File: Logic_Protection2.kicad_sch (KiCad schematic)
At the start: 18 parts

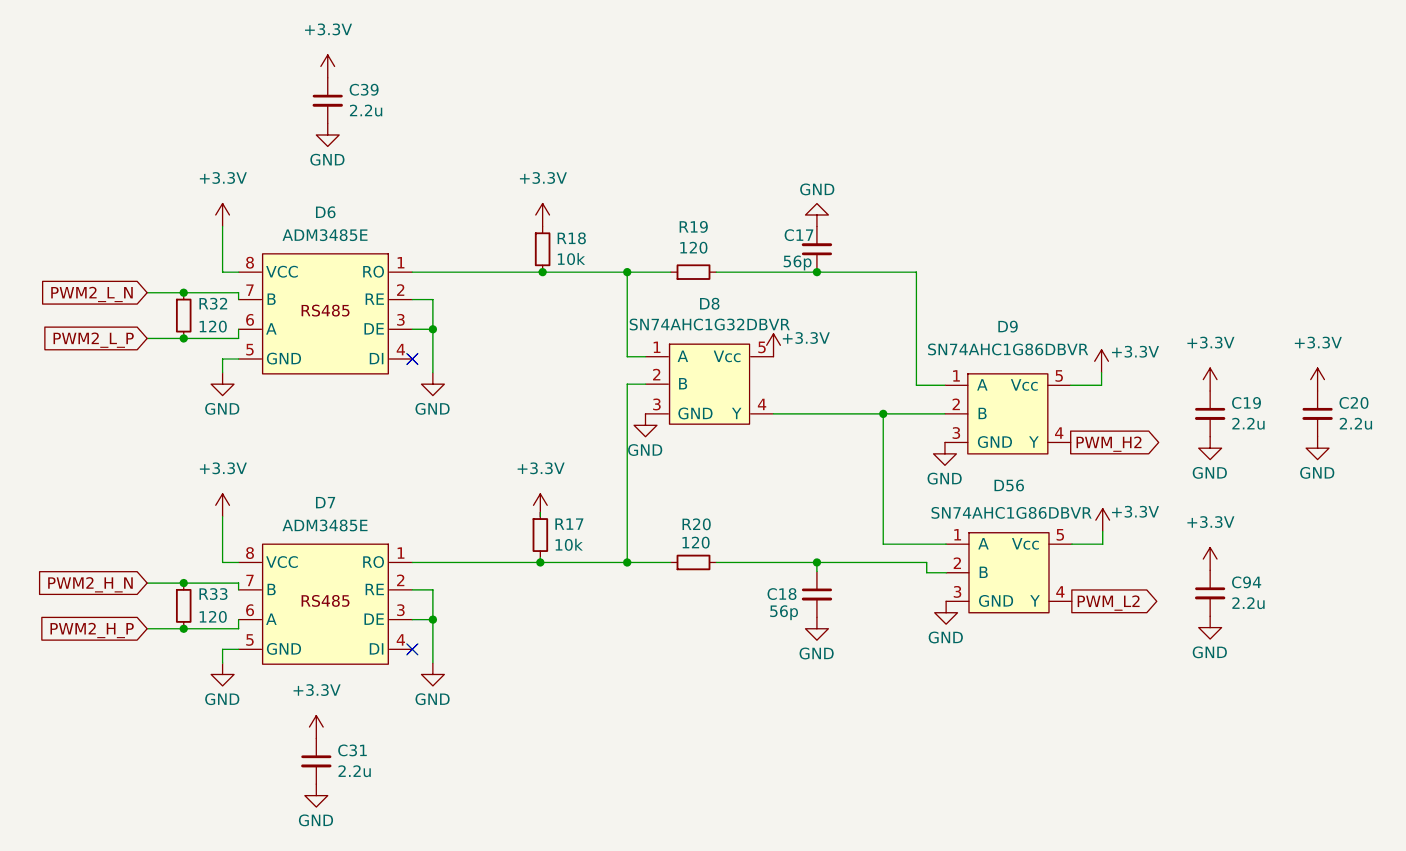
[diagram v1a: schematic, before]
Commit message: Изменил схему
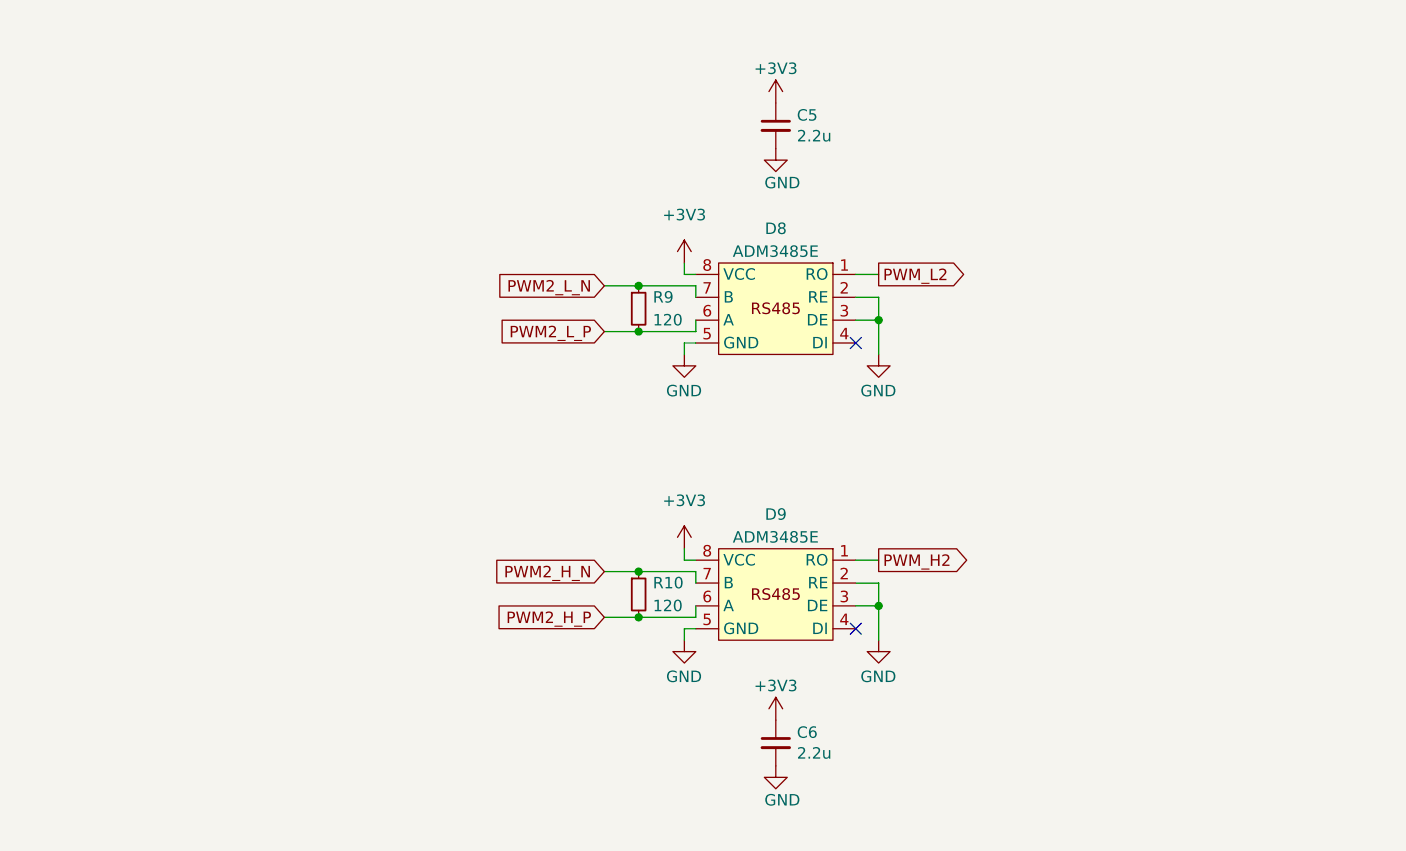
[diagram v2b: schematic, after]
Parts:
- removed C17, C18: 56p, Capacitor_SMD:C_0805_2012Metric_Pad1.18x1.45mm_HandSolder, symbol Device:C_Small
- removed C19, C20, C31, C39, C94: 2.2u, Capacitor_SMD:C_0805_2012Metric_Pad1.18x1.45mm_HandSolder, symbol Device:C_Small
- removed D56, D9: SN74AHC1G86DBVR, Package_TO_SOT_SMD:SOT-23-5_HandSoldering, symbol Logic:SN74AHC1G86DBVR
- removed D6, D7: ADM3485E, Package_SO:SOIC-8_3.9x4.9mm_P1.27mm, symbol Interface_My:ADM3485E
- removed D8: SN74AHC1G32DBVR, Package_TO_SOT_SMD:SOT-23-5_HandSoldering, symbol Logic:SN74AHC1G86DBVR
- removed R17, R18: 10k, Resistor_SMD:R_0805_2012Metric_Pad1.20x1.40mm_HandSolder, symbol Device:R_Small
- removed R19, R20, R32, R33: 120, Resistor_SMD:R_0805_2012Metric_Pad1.20x1.40mm_HandSolder, symbol Device:R_Small
- added C5, C6: 2.2u, Capacitor_SMD:C_0805_2012Metric_Pad1.18x1.45mm_HandSolder, symbol Device:C_Small
- added D8, D9: ADM3485E, Package_SO:SOIC-8_3.9x4.9mm_P1.27mm, symbol Interface_My:ADM3485E_1
- added R10, R9: 120, Resistor_SMD:R_0805_2012Metric_Pad1.20x1.40mm_HandSolder, symbol Device:R_Small
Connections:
- net +3V3: now also C5.1, C6.1, D8.8 (VCC), D9.8 (VCC)
- net GND: now also C5.2, C6.2, D8.2 (RE), D8.3 (DE), D8.5 (GND), D9.2 (RE), D9.3 (DE), D9.5 (GND)
- net PWM2_H_N: now also D9.7 (B), R10.1
- net PWM2_H_P: now also D9.6 (A), R10.2
- net PWM2_L_N: now also D8.7 (B), R9.1
- net PWM2_L_P: now also D8.6 (A), R9.2
- net PWM_H2: now also D9.1 (RO)
- net PWM_L2: now also D8.1 (RO)

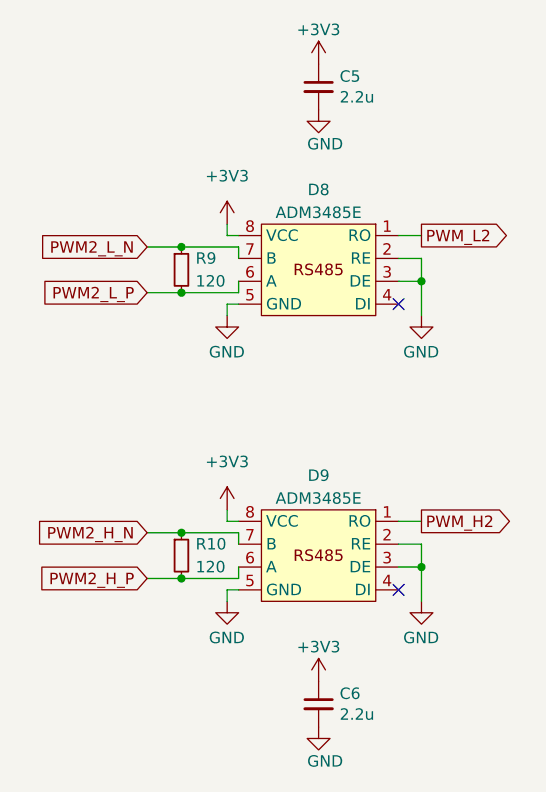
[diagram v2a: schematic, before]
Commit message: Убрал питание 3.3В
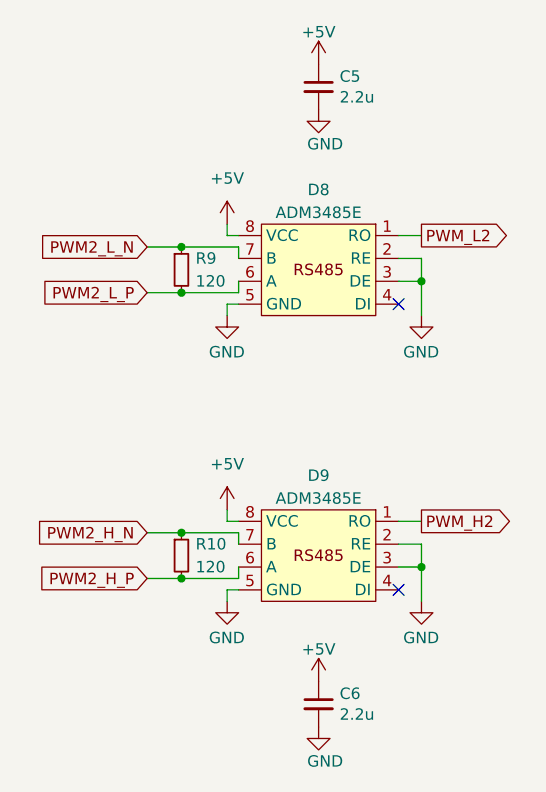
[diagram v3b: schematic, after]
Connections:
- net +3V3 renamed +5V
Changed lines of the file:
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@@
 	)
 	(symbol
-		(lib_id "power:+3.3V")
+		(lib_id "power:+5V")
 		(at 153.67 127 0)
 		(unit 1)
@@
 		(on_board yes)
 		(dnp no)
-		(property "Reference" "#PWR042"
+		(property "Reference" "#PWR42"
 			(at 153.67 130.81 0)
 			(effects
@@
 			)
 		)
-		(property "Value" "+3V3"
-			(at 153.67 123.19 0)
+		(property "Value" "+5V"
+			(at 153.67 123.444 0)
 			(effects
 				(font
@@
 			)
 		)
-		(property "Description" ""
+		(property "Description" "Power symbol creates a global label with name \"+5V\""
 			(at 153.67 127 0)
 			(effects
@@
 			(project "Adapter"
 				(path "/e63e39d7-6ac0-4ffd-8aa3-1841a4541b55/d144a014-f04c-4a5c-ab89-4d35bea7c7d6"
-					(reference "#PWR042")
-					(unit 1)
-				)
-			)
-		)
-	)
-	(symbol
-		(lib_id "power:+3.3V")
+					(reference "#PWR42")
+					(unit 1)
+				)
+			)
+		)
+	)
+	(symbol
+		(lib_id "power:+5V")
 		(at 143.51 76.2 0)
 		(unit 1)
@@
 		(dnp no)
 		(fields_autoplaced yes)
-		(property "Reference" "#PWR017"
+		(property "Reference" "#PWR17"
 			(at 143.51 80.01 0)
 			(effects
@@
 			)
 		)
-		(property "Value" "+3V3"
-			(at 143.51 70.866 0)
+		(property "Value" "+5V"
+			(at 143.51 71.12 0)
 			(effects
 				(font
@@
 			)
 		)
-		(property "Description" ""
+		(property "Description" "Power symbol creates a global label with name \"+5V\""
 			(at 143.51 76.2 0)
 			(effects
@@
 			(project "Adapter"
 				(path "/e63e39d7-6ac0-4ffd-8aa3-1841a4541b55/d144a014-f04c-4a5c-ab89-4d35bea7c7d6"
-					(reference "#PWR017")
+					(reference "#PWR17")
 					(unit 1)
 				)
@@
 	)
 	(symbol
-		(lib_id "power:+3.3V")
+		(lib_id "power:+5V")
 		(at 143.51 107.95 0)
 		(unit 1)
@@
 		(dnp no)
 		(fields_autoplaced yes)
-		(property "Reference" "#PWR021"
+		(property "Reference" "#PWR21"
 			(at 143.51 111.76 0)
 			(effects
@@
 			)
 		)
-		(property "Value" "+3V3"
-			(at 143.51 102.616 0)
+		(property "Value" "+5V"
+			(at 143.51 102.87 0)
 			(effects
 				(font
@@
 			)
 		)
-		(property "Description" ""
+		(property "Description" "Power symbol creates a global label with name \"+5V\""
 			(at 143.51 107.95 0)
 			(effects
@@
 			(project "Adapter"
 				(path "/e63e39d7-6ac0-4ffd-8aa3-1841a4541b55/d144a014-f04c-4a5c-ab89-4d35bea7c7d6"
-					(reference "#PWR021")
+					(reference "#PWR21")
 					(unit 1)
 				)
@@
 	)
 	(symbol
-		(lib_id "power:+3.3V")
+		(lib_id "power:+5V")
 		(at 153.67 58.42 0)
 		(unit 1)
@@
 		(on_board yes)
 		(dnp no)
-		(property "Reference" "#PWR014"
+		(property "Reference" "#PWR14"
 			(at 153.67 62.23 0)
 			(effects
@@
 			)
 		)
-		(property "Value" "+3V3"
-			(at 153.67 54.61 0)
+		(property "Value" "+5V"
+			(at 153.67 54.864 0)
 			(effects
 				(font
@@
 			)
 		)
-		(property "Description" ""
+		(property "Description" "Power symbol creates a global label with name \"+5V\""
 			(at 153.67 58.42 0)
 			(effects
@@
 			(project "Adapter"
 				(path "/e63e39d7-6ac0-4ffd-8aa3-1841a4541b55/d144a014-f04c-4a5c-ab89-4d35bea7c7d6"
-					(reference "#PWR014")
-					(unit 1)
-				)
+					(reference "#PWR14")
+					(unit 1)
+				)

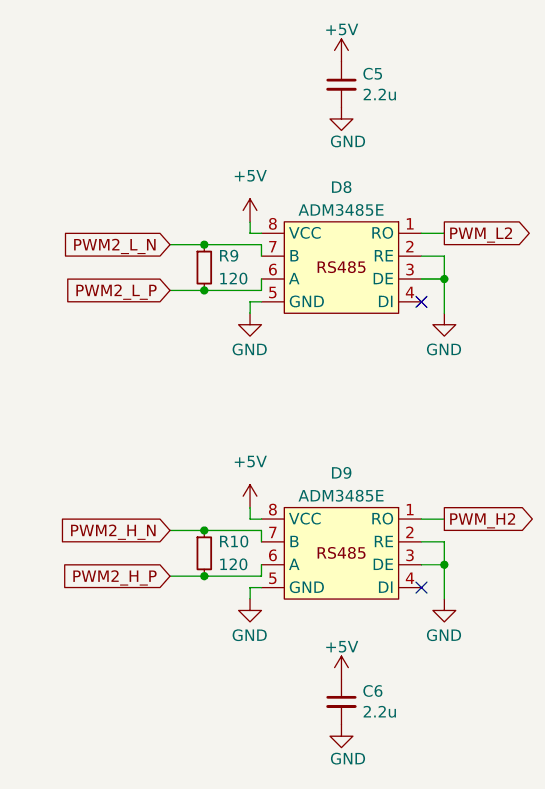
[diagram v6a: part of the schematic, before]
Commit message: Изменения: добавил подтяжки шины RS485
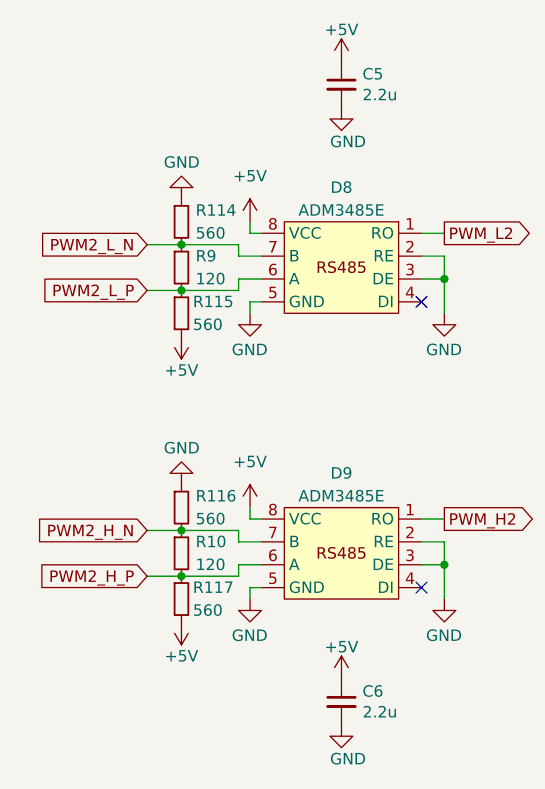
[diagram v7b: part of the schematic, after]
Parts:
- added R114, R115, R116, R117: 560, Resistor_SMD:R_0805_2012Metric_Pad1.20x1.40mm_HandSolder, symbol Device:R_Small
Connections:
- net +5V: now also R115.2, R117.2
- net GND: now also R114.1, R116.1
- net PWM2_H_N: now also R116.2
- net PWM2_H_P: now also R117.1
- net PWM2_L_N: now also R114.2
- net PWM2_L_P: now also R115.1
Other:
- moved on the sheet: R10, R9
